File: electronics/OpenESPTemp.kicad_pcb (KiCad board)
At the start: 2 copper layers, 15 x 63 mm, 42 parts, among them J2 Qwiic_RA, Q1 TSM260P02CX-RFG, Q2 DMN2020LSN-7, SW1 WAKE, SW2 FCT, SW3 BOOT, SW4 RESET, U2 RV-3028-C7, U3 BME280, U4 TLV70033_SOT23-5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

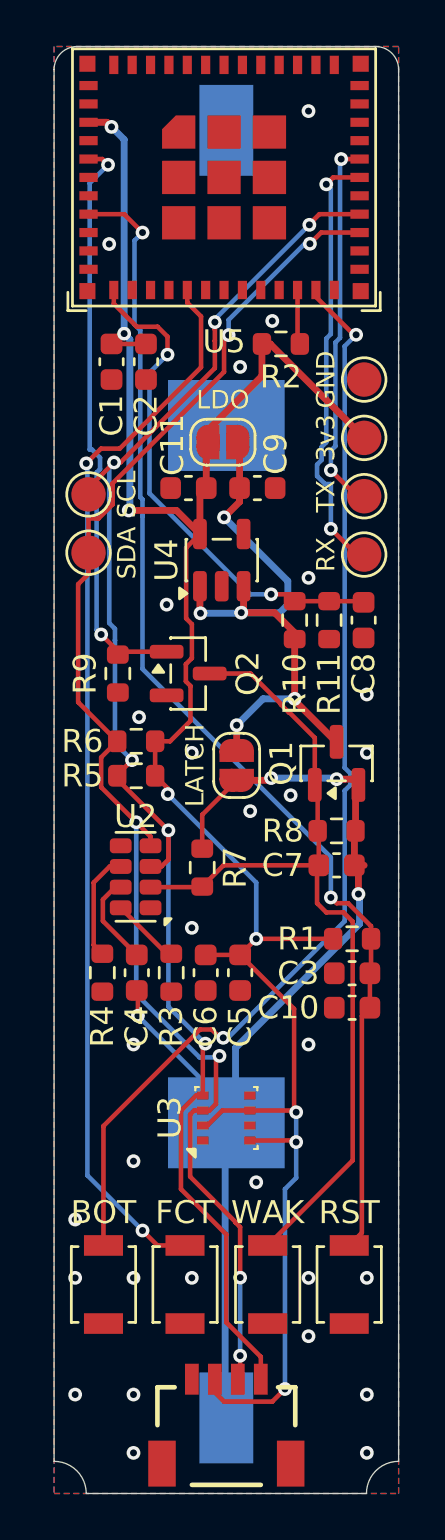
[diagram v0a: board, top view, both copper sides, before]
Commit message: Fix Pcb issues
- Fix wrong connection of C4
- Move symbol lib into libs/; Delete unused .kicad_sch file
- Make LDO Solder Jumper Bridged by default
- Fix temp notes file (Licenses.txt)
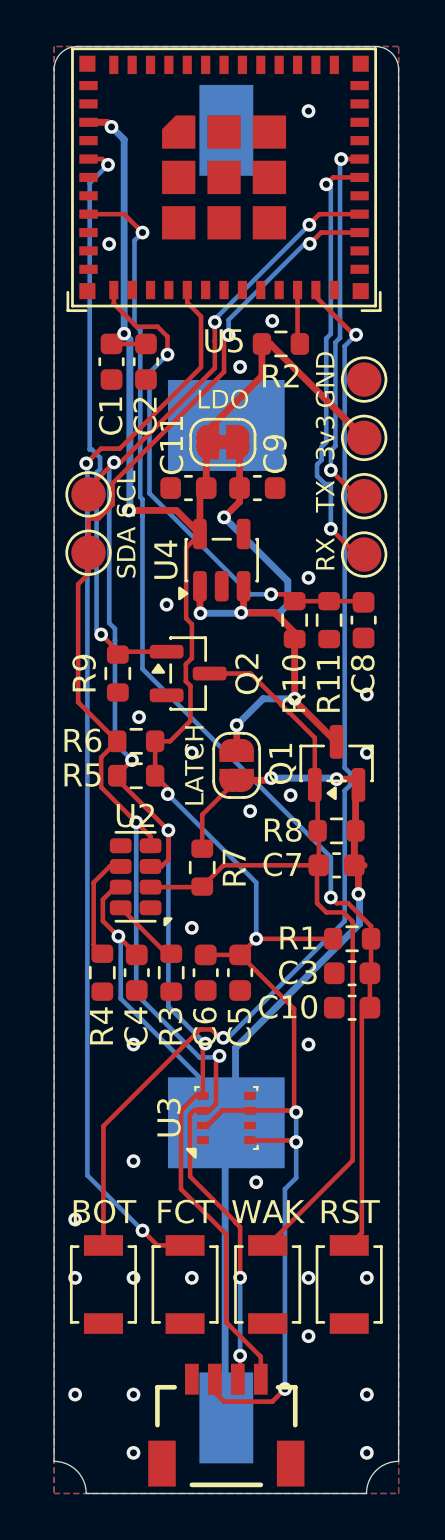
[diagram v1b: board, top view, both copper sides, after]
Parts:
- JP2: footprint Jumper:SolderJumper-2_P1.3mm_Open_RoundedPad1.0x1.5mm -> Jumper:SolderJumper-2_P1.3mm_Bridged_RoundedPad1.0x1.5mm
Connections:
- C4 pad 1: Net-(U2-VDD) -> +BATT
- C4 pad 2: +BATT -> GND
- U2 pad 7: Net-(U2-VDD) -> +BATT
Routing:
- net +BATT: track 47.0 -> 53.7 mm
- net Net-(U2-VDD): track 4.02 -> 0.00 mm
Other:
- board text added: "OpenESPTemp v2.0.1"
- board text removed: "OpenESPTemp v2.0"

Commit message: fix(electronics): Improve Schematic
Improve schematic overall
Add exported .pdf of current schematics
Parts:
- turned R6 to 180 degrees
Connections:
- R6 pad 1: SDA -> +3V3
- R6 pad 2: +3V3 -> SDA
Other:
- board text added: "OpenESPTemp v2.1.0"
- board text removed: "OpenESPTemp v2.0.1"
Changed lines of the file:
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@@
 	(footprint "Resistor_SMD:R_0603_1608Metric"
 		(layer "F.Cu")
-		(at 92.075 69.75)
+		(at 92.075 69.75 180)
 		(descr "Resistor SMD 0603 (1608 Metric), square (rectangular) end terminal, IPC-7351 nominal, (Body size source: IPC-SM-782 page 72, https://www.pcb-3d.com/wordpress/wp-content/uploads/ipc-sm-782a_amendment_1_and_2.pdf), generated with kicad-footprint-generator")
 		(tags "resistor")
 		(property "Reference" "R6"
-			(at -1.43 0 0)
+			(at 1.43 0 0)
 			(layer "F.SilkS")
 			(effects
@@
 		)
 		(property "MFR" "MCT06030C4701FP500"
-			(at 0 0 0)
+			(at 0 0 180)
 			(unlocked yes)
 			(layer "F.Fab")
@@
 		(attr smd)
 		(fp_line
+			(start -0.237258 0.5225)
+			(end 0.237258 0.5225)
+			(stroke
+				(width 0.12)
+				(type solid)
+			)
+			(layer "F.SilkS")
+		)
+		(fp_line
 			(start -0.237258 -0.5225)
 			(end 0.237258 -0.5225)
-			(stroke
-				(width 0.12)
-				(type solid)
-			)
-			(layer "F.SilkS")
-		)
-		(fp_line
-			(start -0.237258 0.5225)
-			(end 0.237258 0.5225)
 			(stroke
 				(width 0.12)
@@
 		)
 		(pad "1" smd roundrect
-			(at -0.825 0)
+			(at -0.825 0 180)
+			(size 0.8 0.95)
+			(layers "F.Cu" "F.Mask" "F.Paste")
+			(roundrect_rratio 0.25)
+			(net 3 "+3V3")
+			(pintype "passive")
+		)
+		(pad "2" smd roundrect
+			(at 0.825 0 180)
 			(size 0.8 0.95)
 			(layers "F.Cu" "F.Mask" "F.Paste")
 			(roundrect_rratio 0.25)
 			(net 10 "SDA")
-			(pintype "passive")
-		)
-		(pad "2" smd roundrect
-			(at 0.825 0)
-			(size 0.8 0.95)
-			(layers "F.Cu" "F.Mask" "F.Paste")
-			(roundrect_rratio 0.25)
-			(net 3 "+3V3")
 			(pintype "passive")
 		)
@@
 		)
 	)
-	(gr_text "OpenESPTemp\nv2.0.1"
+	(gr_text "OpenESPTemp\nv2.1.0"
 		(at 96 65.8825 90)
 		(layer "B.SilkS")
